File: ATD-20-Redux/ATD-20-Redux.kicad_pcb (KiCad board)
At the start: 2 copper layers, 21.8 x 56.6 mm, 5 parts, among them J1 RTC Pins, U1 DS1315, Y1 32.768 KHz

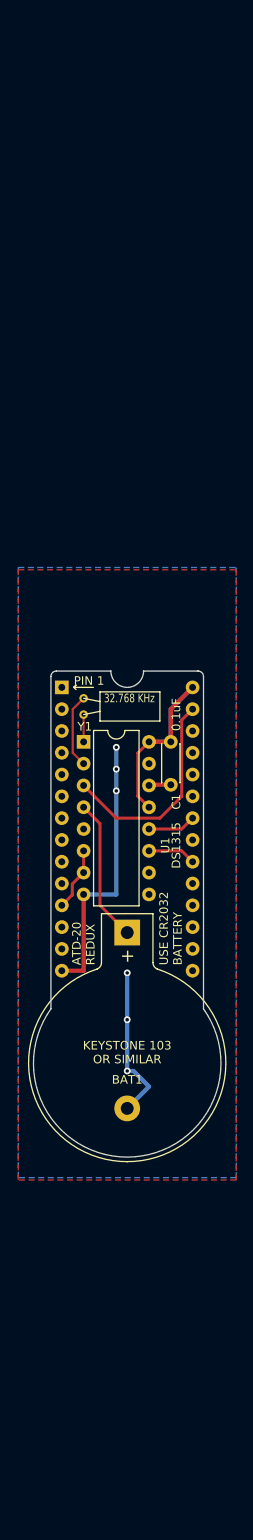
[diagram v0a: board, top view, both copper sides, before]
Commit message: Flipped layout of ATD-20 Redux so battery was at other end. This is to make it easier to change the battery. The battery holder is also slightly off-center to allow battery holder pin to fit between chips on the T512K board, in case someone has their chips socketed on their board.
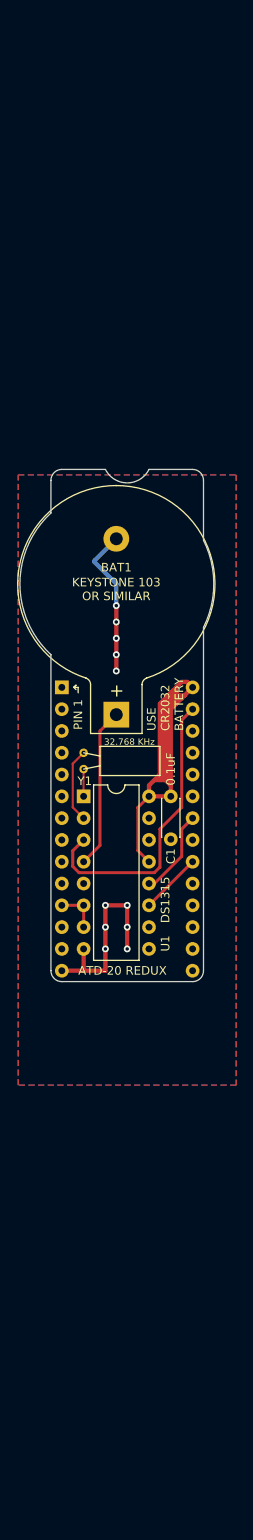
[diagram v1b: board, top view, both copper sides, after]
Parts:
- moved BAT1 25.4 mm to (117.5, 60.3), turned to 90 degrees
- moved C1 6.35 mm to (123.8, 69.8)
- moved U1 6.35 mm to (113.7, 69.8)
- moved Y1 6.35 mm to (113.7, 66.7)
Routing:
- net VCC: track 28.6 -> 64.3 mm
- net GND: track 53.3 -> 40.4 mm, vias 6 -> 11
- net /~IOW: track 24.7 -> 34.3 mm
- net /~IOR: track 5.61 -> 10.1 mm
- net /D0: track 7.40 -> 5.08 mm
- net Net-(BAT1-Pad1): track 16.7 -> 18.7 mm
- net /~CS_RTC: track 5.61 -> 7.18 mm
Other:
- board size 21.8 x 56.6 mm -> 22.6 x 59.7 mm
- board text added: "Board layout by Jayeson Lee-Steere and placed into the public domain"
- board text added: "Circuit is the reference design from the DS1315 datasheet and confirmed to match a real DS1216-C SmartWatch"
- board text added: "https://github.com/ JayesonLS/SmartWatchRedux"
- board text removed: "Circuit is the reference design from the DS1315 datasheet and confirmed to match a real DS1216-C SmartWatch. Board layout by Jayeson Lee-Steere and placed into the public domain."
- board text removed: "TRIM FLUSH BEFORE SOLDERING"
- board text removed: "https://github.com/ JayesonLS/TandyCircuitsAndLogic/ tree/master/ATD-20-Redux"

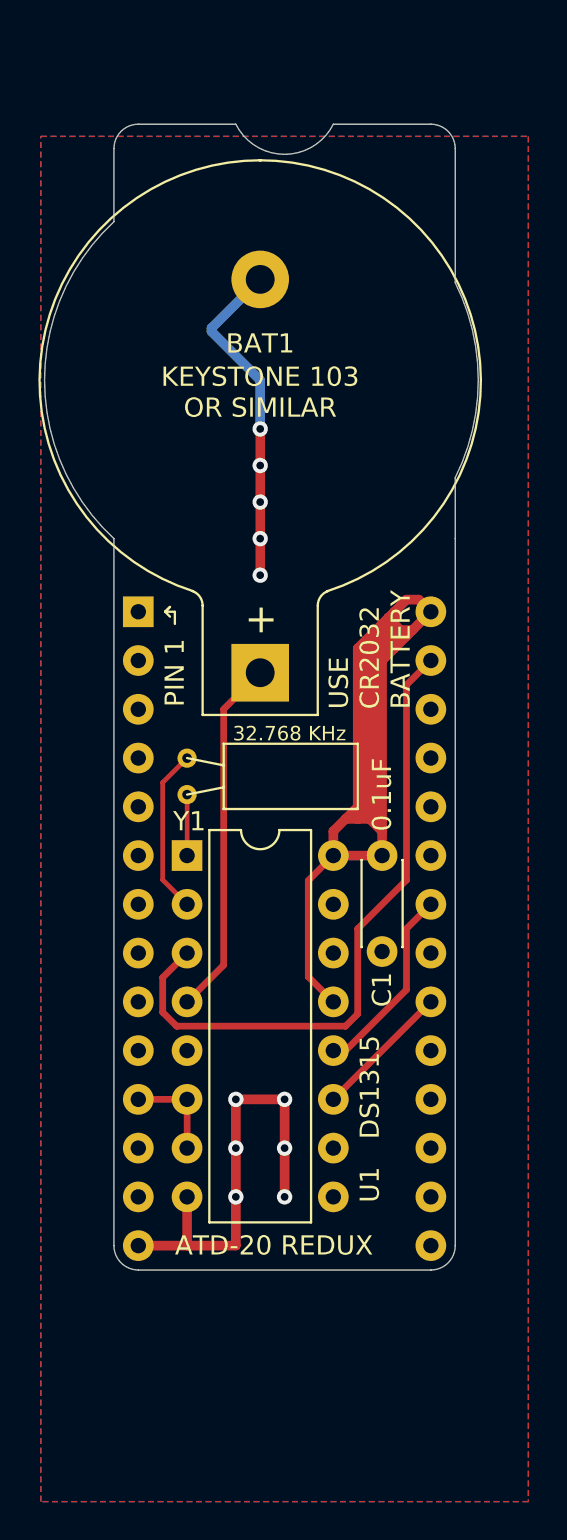
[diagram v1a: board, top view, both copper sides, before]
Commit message: Change battery holder on ATD-20-Redux to something that is not as tall. This is to increase the distance between the battery and the adjacent board.
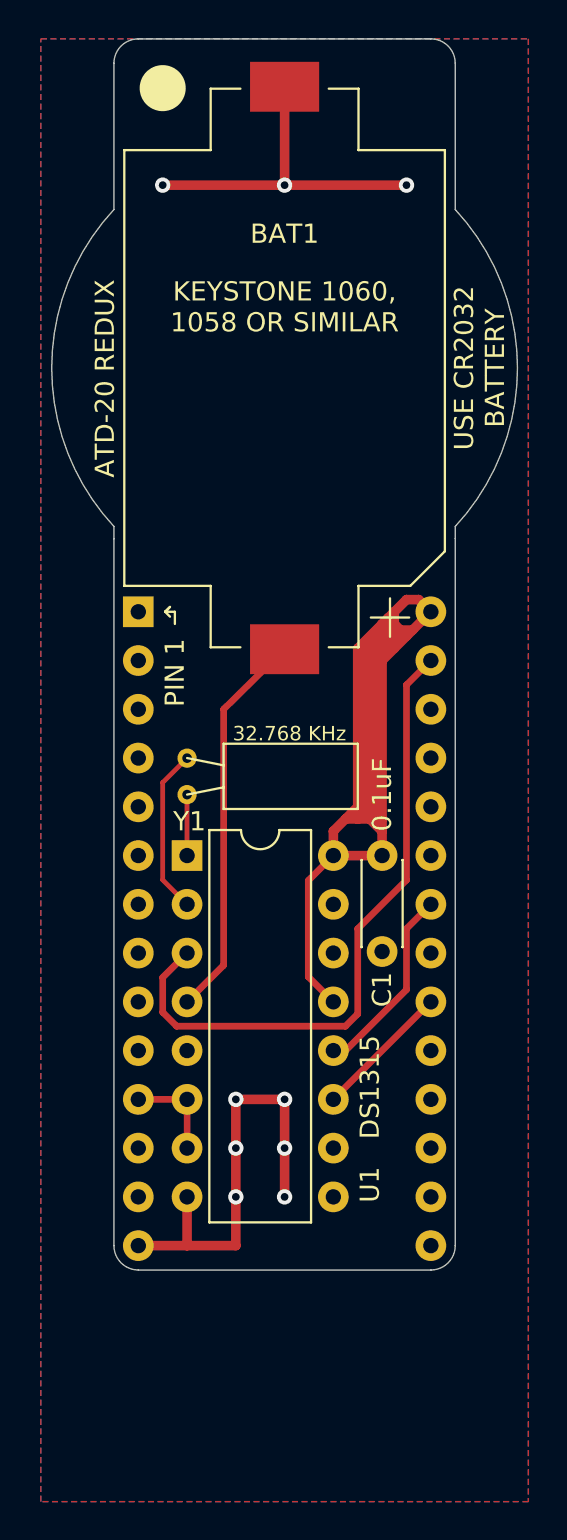
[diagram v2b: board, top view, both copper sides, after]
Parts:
- BAT1: footprint Battery:BatteryHolder_Keystone_103_1x20mm -> Battery:BatteryHolder_Keystone_1060_1x2032
- moved BAT1 15.9 mm to (118.7, 44.5)
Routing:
- net Net-(BAT1-Pad1): track 18.7 -> 20.5 mm
- net GND: track 40.4 -> 40.7 mm, vias 11 -> 9
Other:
- board size 22.6 x 59.7 mm -> 24.3 x 64.1 mm
- board text added: "KEYSTONE 1060, 1058 OR SIMILAR"
- board text added: "REV 1.1"
- board text removed: "KEYSTONE 103 OR SIMILAR"
- board text removed: "REV 1.0"

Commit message: Minor tweaks to ATD-20-Redux.
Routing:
- net GND: track 40.7 -> 59.7 mm, vias 9 -> 11
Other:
- board text added: "Circuit is the reference design from the DS1315 datasheet Board layout by Jayeson Lee-Steere and placed into the public domain"
- board text removed: "Board layout by Jayeson Lee-Steere and placed into the public domain"
- board text removed: "Circuit is the reference design from the DS1315 datasheet and confirmed to match a real DS1216-C SmartWatch"
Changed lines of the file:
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@@
   (general
     (thickness 1.6)
-    (drawings 29)
-    (tracks 86)
+    (drawings 28)
+    (tracks 90)
     (zones 0)
     (modules 5)
@@
       (plotvalue true)
       (plotinvisibletext false)
-      (padsonsilk true)
+      (padsonsilk false)
       (subtractmaskfromsilk false)
       (outputformat 1)
@@
   (gr_arc (start 118.745 44.45) (end 127.634999 52.704999) (angle -85.75780721) (layer Edge.Cuts) (width 0.05))
   (gr_line (start 126.365 27.305) (end 111.125 27.305) (layer Edge.Cuts) (width 0.05))
-  (gr_text "Board layout\nby Jayeson Lee-Steere\nand placed into\nthe public domain" (at 113.03 45.085 270) (layer B.SilkS)
-    (effects (font (size 1 0.9) (thickness 0.15)) (justify mirror))
-  )
   (gr_line (start 113.03 57.15) (end 113.03 57.785) (layer F.SilkS) (width 0.12))
   (gr_line (start 112.522 57.15) (end 113.03 57.15) (layer F.SilkS) (width 0.12))
-  (gr_text "https://github.com/\nJayesonLS/SmartWatchRedux" (at 117.475 73.66 -90) (layer B.SilkS)
+  (gr_text "https://github.com/\nJayesonLS/SmartWatchRedux" (at 117.475 70.485 -90) (layer B.SilkS)
     (effects (font (size 1 1) (thickness 0.15)) (justify mirror))
   )
@@
     (effects (font (size 1 1) (thickness 0.15)) (justify left mirror))
   )
-  (gr_text "Circuit is the reference\ndesign from the DS1315\ndatasheet and confirmed\nto match a real DS1216-C\nSmartWatch " (at 122.555 45.085 270) (layer B.SilkS)
-    (effects (font (size 1 0.9) (thickness 0.15)) (justify mirror))
+  (gr_text "Circuit is the reference design\nfrom the DS1315 datasheet\n\nBoard layout by Jayeson \nLee-Steere and  placed \ninto the public domain" (at 118.745 50.8 -90) (layer B.SilkS)
+    (effects (font (size 1 0.9) (thickness 0.15)) (justify left mirror))
   )
   (gr_text "\nATD-20 REDUX" (at 108.585 50.165 90) (layer F.SilkS)
@@
   (via (at 118.745 87.63) (size 0.8) (drill 0.4) (layers F.Cu B.Cu) (net 2))
   (segment (start 118.745 85.09) (end 118.745 87.63) (width 0.5) (layer F.Cu) (net 2))
-  (segment (start 118.745 29.8) (end 118.745 34.925) (width 0.5) (layer F.Cu) (net 2))
-  (via (at 112.395 34.925) (size 0.8) (drill 0.4) (layers F.Cu B.Cu) (net 2))
-  (segment (start 118.745 34.925) (end 112.395 34.925) (width 0.5) (layer F.Cu) (net 2))
-  (via (at 125.095 34.925) (size 0.8) (drill 0.4) (layers F.Cu B.Cu) (net 2))
-  (segment (start 118.745 34.925) (end 125.095 34.925) (width 0.5) (layer F.Cu) (net 2))
-  (via (at 118.745 34.925) (size 0.8) (drill 0.4) (layers F.Cu B.Cu) (net 2))
+  (via (at 112.395 53.975) (size 0.8) (drill 0.4) (layers F.Cu B.Cu) (net 2))
+  (segment (start 118.745 53.975) (end 115.57 53.975) (width 0.5) (layer F.Cu) (net 2))
+  (via (at 125.095 53.975) (size 0.8) (drill 0.4) (layers F.Cu B.Cu) (net 2))
+  (segment (start 118.745 53.975) (end 121.92 53.975) (width 0.5) (layer F.Cu) (net 2))
+  (via (at 118.745 53.975) (size 0.8) (drill 0.4) (layers F.Cu B.Cu) (net 2))
+  (segment (start 118.745 29.8) (end 118.745 53.975) (width 0.5) (layer F.Cu) (net 2))
+  (segment (start 121.92 53.975) (end 125.095 53.975) (width 0.5) (layer F.Cu) (net 2))
+  (via (at 121.92 53.975) (size 0.8) (drill 0.4) (layers F.Cu B.Cu) (net 2))
+  (segment (start 115.57 53.975) (end 112.395 53.975) (width 0.5) (layer F.Cu) (net 2))
+  (via (at 115.57 53.975) (size 0.8) (drill 0.4) (layers F.Cu B.Cu) (net 2))
   (segment (start 121.285 69.85) (end 123.825 69.85) (width 0.5) (layer F.Cu) (net 3))
   (segment (start 119.980009 76.165009) (end 121.285 77.47) (width 0.35) (layer F.Cu) (net 3))
@@
     (polygon
       (pts
-        (xy 131.445 103.505) (xy 106.045 103.505) (xy 106.045 27.305) (xy 131.445 27.305)
+        (xy 131.445 128.730632) (xy 106.045 128.730632) (xy 106.045 52.530632) (xy 131.445 52.530632)
       )
     )
@@
     (polygon
       (pts
-        (xy 131.445 103.505) (xy 106.045 103.505) (xy 106.045 27.305) (xy 131.445 27.305)
+        (xy 131.445 154.512831) (xy 106.045 154.512831) (xy 106.045 78.312831) (xy 131.445 78.312831)
       )
     )
   )
-  (zone (net 0) (net_name "") (layer F.Cu) (hatch edge 0.508)
-    (connect_pads (clearance 0.635))
+  (zone (net 2) (net_name GND) (layer F.Cu) (hatch edge 0.508)
+    (connect_pads no (clearance 0.635))
     (min_thickness 0.254)
-    (keepout (tracks allowed) (vias allowed) (copperpour not_allowed))
-    (fill (arc_segments 32) (thermal_gap 0.508) (thermal_bridge_width 0.508))
+    (fill yes (arc_segments 32) (thermal_gap 0.508) (thermal_bridge_width 0.508))
     (polygon
       (pts
-        (xy 127.635 78.74) (xy 109.855 78.74) (xy 109.855 58.42) (xy 127.635 58.42)
+        (xy 131.445 55.245) (xy 106.045 55.245) (xy 106.045 -20.955) (xy 131.445 -20.955)
       )
     )
